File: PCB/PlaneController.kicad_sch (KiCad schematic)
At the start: 13 parts, among them J1 Conn_01x06_Pin, J2 Conn_01x04_Pin, J3 Conn_01x03, M1 Motor_Servo, M2 Motor_Servo, M3 Motor_Servo, M4 Motor_Servo, M5 Motor_Servo

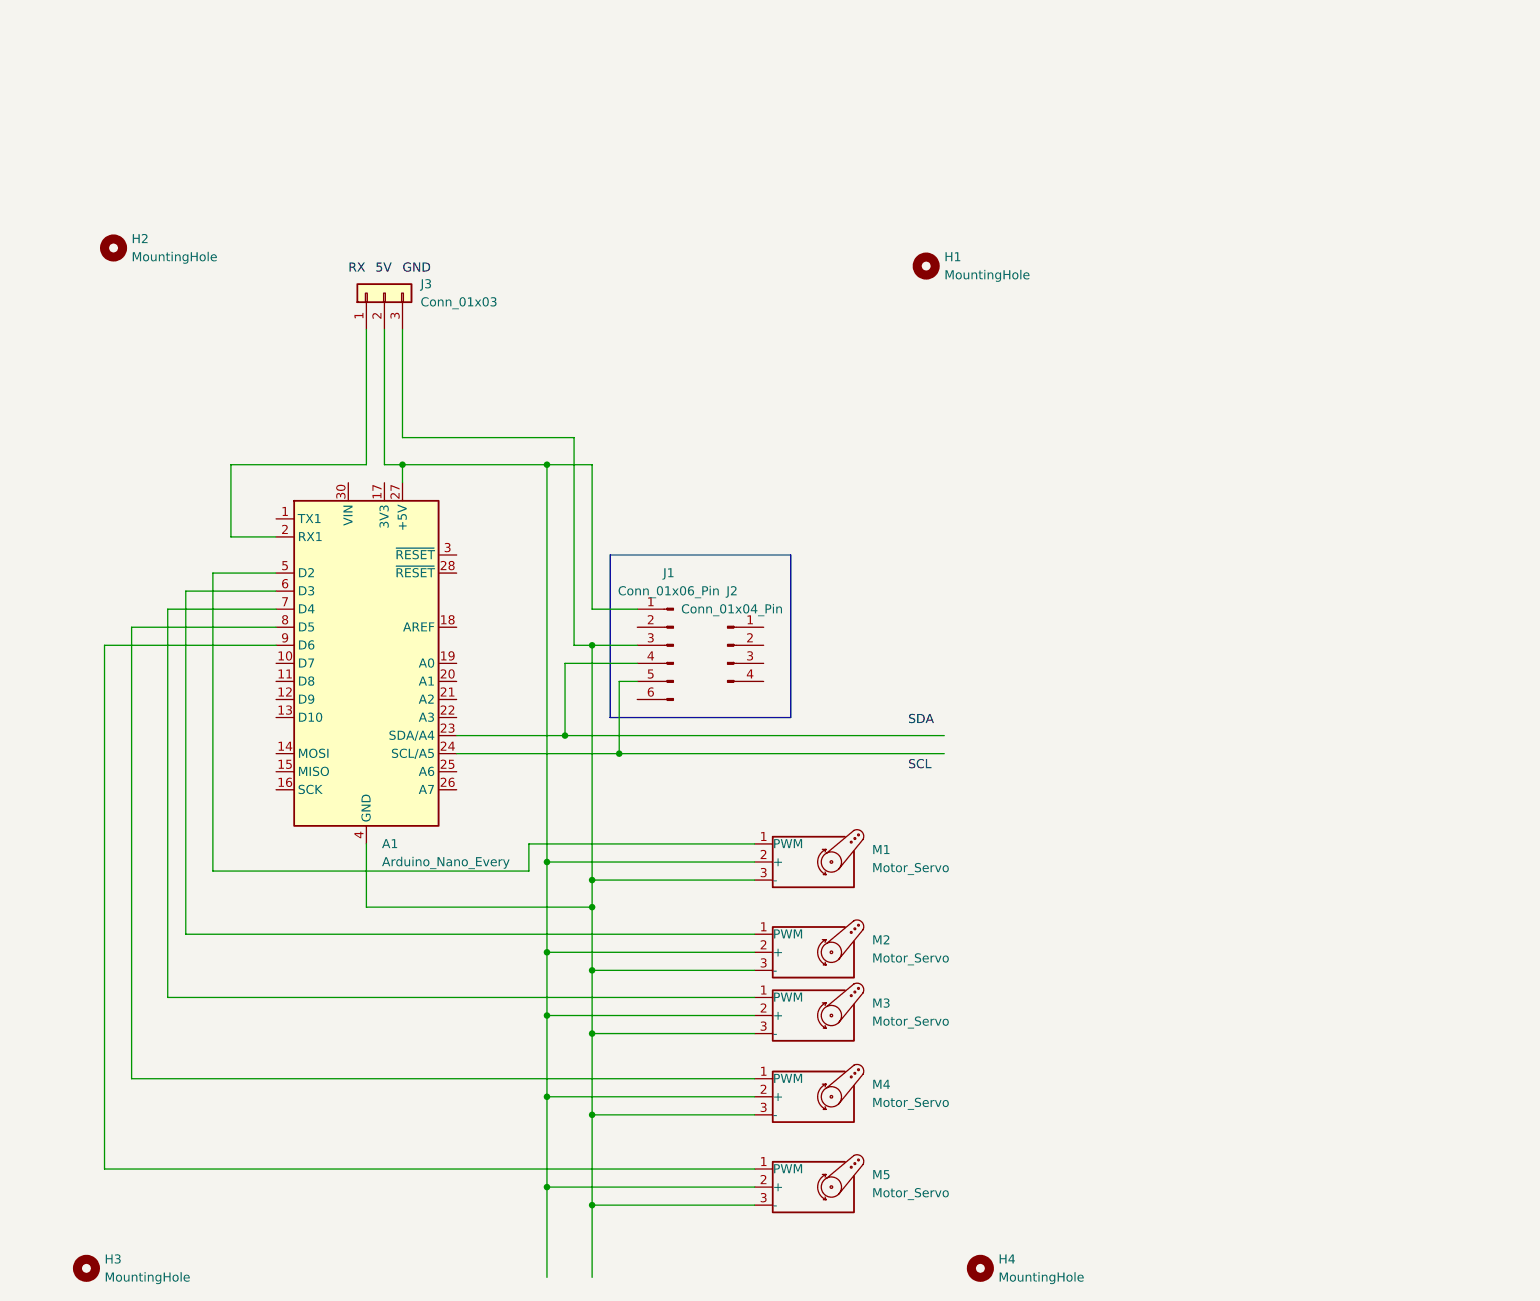
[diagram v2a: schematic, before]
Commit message: Add PCB traces for CC1101 radio
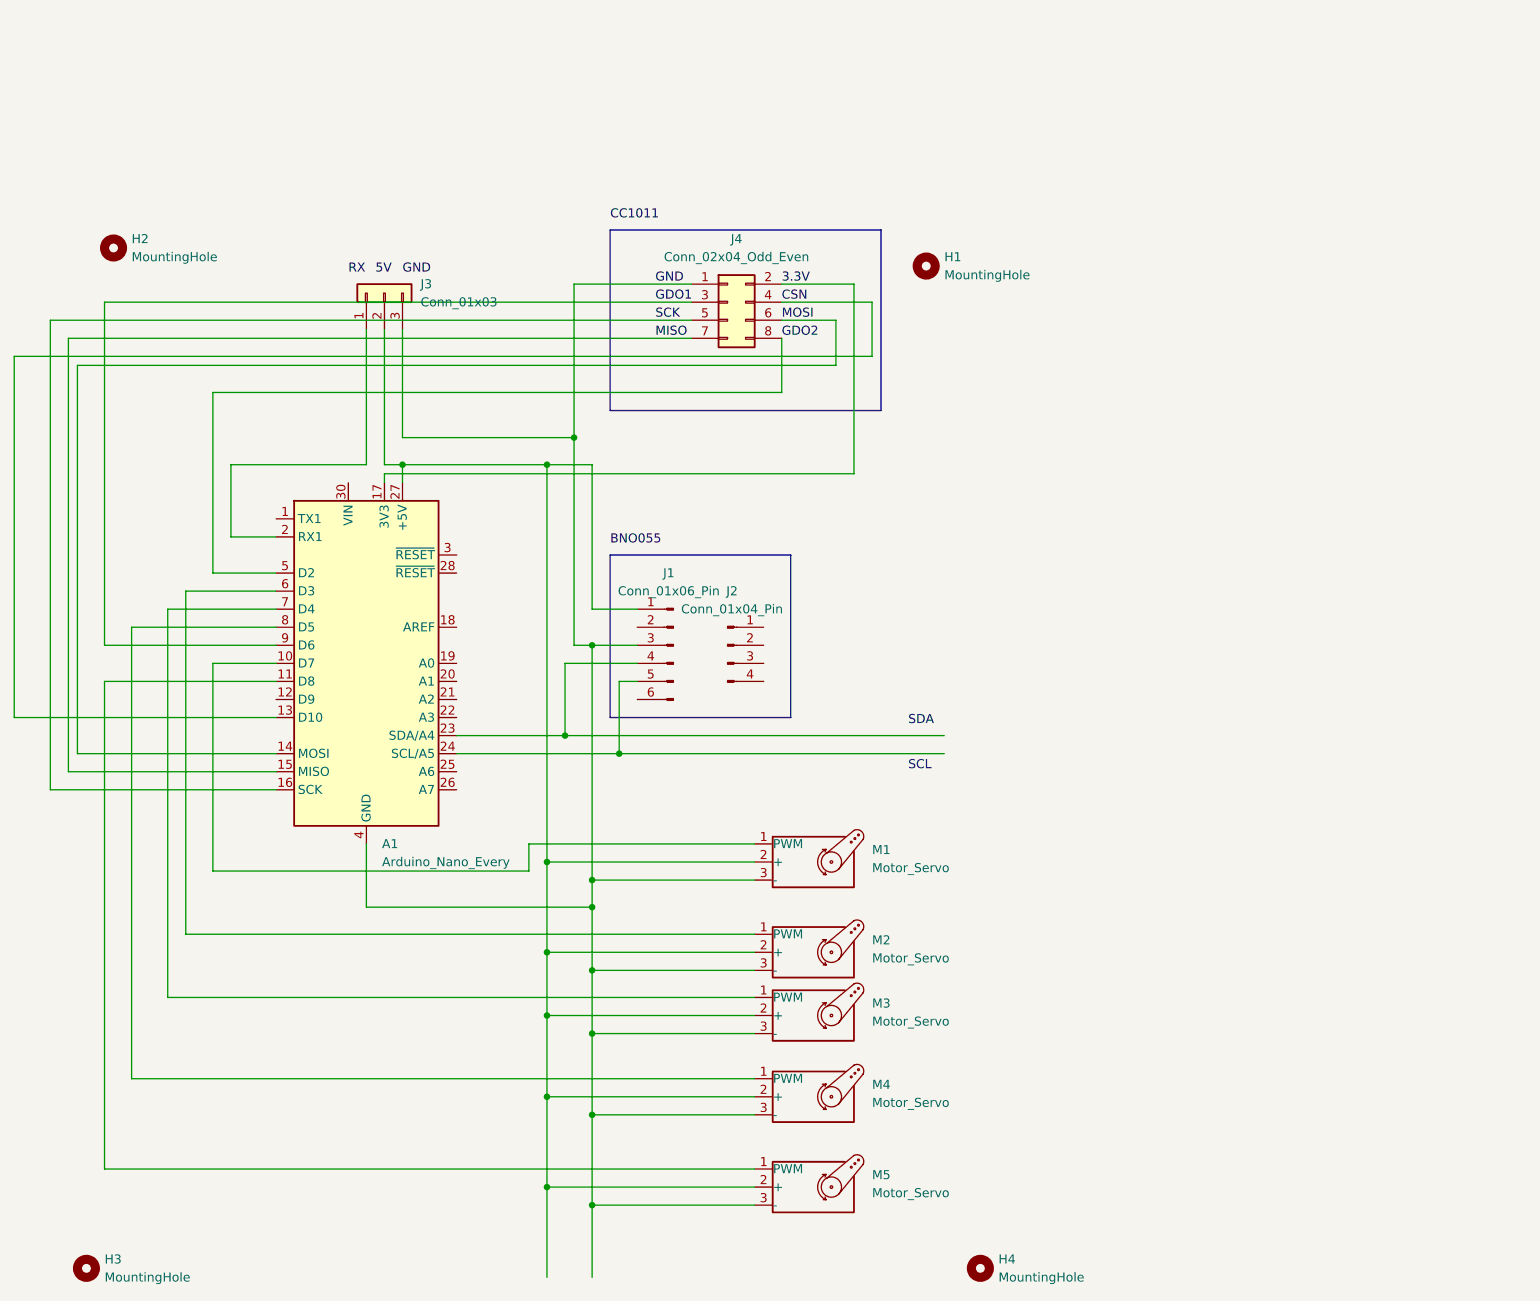
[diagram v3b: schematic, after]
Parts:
- added J4: Conn_02x04_Odd_Even, Connector_PinSocket_2.54mm:PinSocket_2x04_P2.54mm_Vertical, symbol Connector_Generic:Conn_02x04_Odd_Even
- J1: footprint Connector_PinHeader_2.54mm:PinHeader_1x06_P2.54mm_Vertical -> Connector_PinSocket_2.54mm:PinSocket_1x06_P2.54mm_Vertical
- J2: footprint Connector_PinHeader_2.54mm:PinHeader_1x04_P2.54mm_Vertical -> Connector_PinSocket_2.54mm:PinSocket_1x04_P2.54mm_Vertical
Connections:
- net GND: now also A1.29 (GND), A1.4 (GND), J1.3 (Pin_3), J3.3 (Pin_3), M1.3 (-), M2.3 (-), M3.3 (-), M4.3 (-), M5.3 (-), J4.1 (Pin_1)
- net at M5.1 (PWM): now also A1.11 (D8); no longer A1.9 (D6)
- net at M1.1 (PWM): now also A1.10 (D7); no longer A1.5 (D2)
- net CSN: now reaches A1.13 (D10)
- net CSN: now also J4.4 (Pin_4)
- net MOSI: now reaches A1.14 (MOSI)
- net MOSI: now also J4.6 (Pin_6)
- net MISO: now reaches A1.15 (MISO)
- net MISO: now also J4.7 (Pin_7)
- net SCK: now reaches A1.16 (SCK)
- net SCK: now also J4.5 (Pin_5)
- net 3.3V: now reaches A1.17 (3V3)
- net 3.3V: now also J4.2 (Pin_2)
- new net GDO1: A1.9 (D6), J4.3 (Pin_3)
- new net GDO2: A1.5 (D2), J4.8 (Pin_8)

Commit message: Major PCB fix
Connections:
- net GDO1 renamed GDO1 / GDO0
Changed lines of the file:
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@@
-	(wire
-		(pts
-			(xy 118.11 53.34) (xy 35.56 53.34)
-		)
-		(stroke
-			(width 0)
-			(type default)
-		)
-	)
 	(wire
 		(pts
@@
 		(pts
 			(xy 97.79 76.2) (xy 97.79 132.08)
+		)
+		(stroke
+			(width 0)
+			(type default)
+		)
+	)
+	(wire
+		(pts
+			(xy 35.56 53.34) (xy 118.11 53.34)
 		)
 		(stroke
@@
 	)
 	(rectangle
-		(start 106.68 43.18)
+		(start 102.87 43.18)
 		(end 144.78 68.58)
 		(stroke
@@
 	)
 	(label "CC1011"
-		(at 106.68 41.91 0)
+		(at 102.87 41.91 0)
 		(fields_autoplaced yes)
 		(effects
@@
 		)
 	)
-	(label "GDO1"
-		(at 113.03 53.34 0)
-		(fields_autoplaced yes)
-		(effects
+	(label "GDO1 {slash} GDO0"
+		(at 104.14 53.34 0)
+		(fields_autoplaced yes)
+		(effects

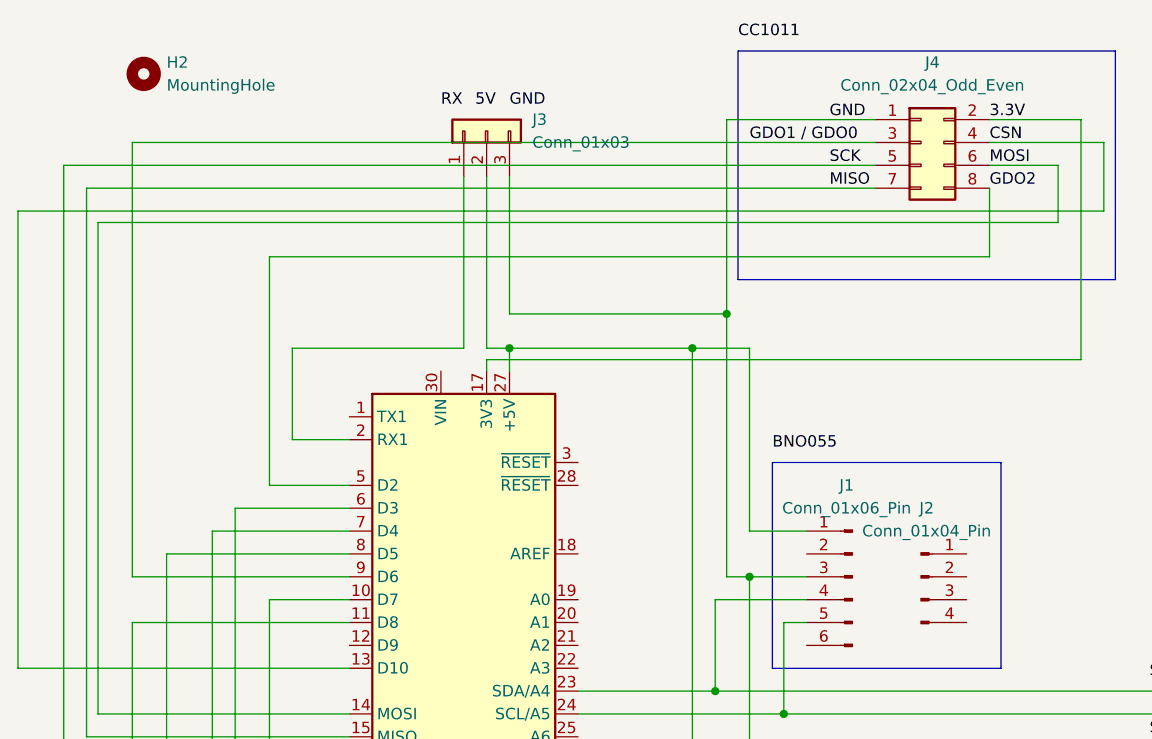
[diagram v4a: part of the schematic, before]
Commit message: Radio is now connected and unnecessary connections are removed from the pcb
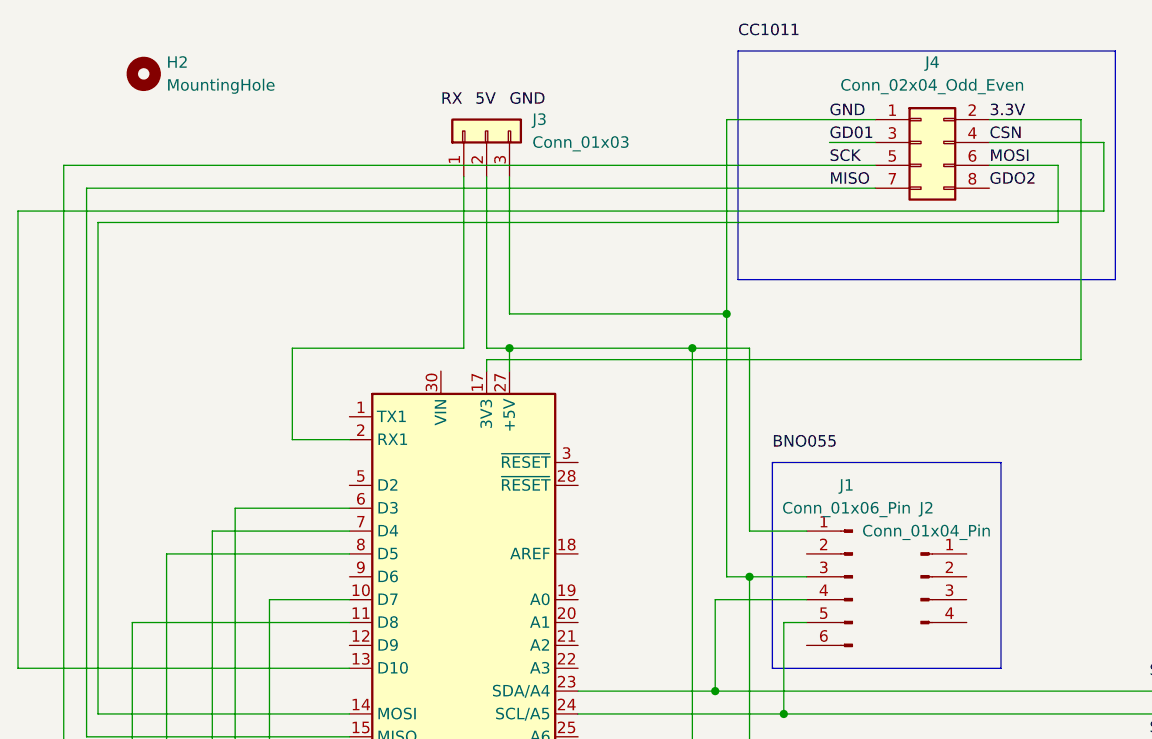
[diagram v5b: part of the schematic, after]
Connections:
- net GDO2: no longer A1.5 (D2)
- net GDO1 / GDO0: no longer names the net of A1.9 (D6)
- net GDO1 / GDO0: no longer J4.3 (Pin_3)
- new net GD01: J4.3 (Pin_3)
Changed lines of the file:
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@@
-	(wire
-		(pts
-			(xy 130.81 58.42) (xy 130.81 66.04)
-		)
-		(stroke
-			(width 0)
-			(type default)
-		)
-	)
 	(wire
 		(pts
@@
 	(wire
 		(pts
-			(xy 35.56 101.6) (xy 59.69 101.6)
-		)
-		(stroke
-			(width 0)
-			(type default)
-		)
-	)
-	(wire
-		(pts
 			(xy 97.79 144.78) (xy 97.79 153.67)
 		)
@@
 	(wire
 		(pts
+			(xy 113.03 53.34) (xy 118.11 53.34)
+		)
+		(stroke
+			(width 0)
+			(type default)
+		)
+	)
+	(wire
+		(pts
 			(xy 104.14 180.34) (xy 127 180.34)
 		)
@@
 	(wire
 		(pts
-			(xy 130.81 66.04) (xy 50.8 66.04)
-		)
-		(stroke
-			(width 0)
-			(type default)
-		)
-	)
-	(wire
-		(pts
 			(xy 101.6 101.6) (xy 104.14 101.6)
 		)
@@
 	(wire
 		(pts
-			(xy 50.8 91.44) (xy 59.69 91.44)
-		)
-		(stroke
-			(width 0)
-			(type default)
-		)
-	)
-	(wire
-		(pts
 			(xy 127 151.13) (xy 44.45 151.13)
 		)
@@
 	(wire
 		(pts
-			(xy 50.8 66.04) (xy 50.8 91.44)
-		)
-		(stroke
-			(width 0)
-			(type default)
-		)
-	)
-	(wire
-		(pts
 			(xy 143.51 60.96) (xy 143.51 53.34)
 		)
@@
 	(wire
 		(pts
-			(xy 35.56 53.34) (xy 35.56 101.6)
-		)
-		(stroke
-			(width 0)
-			(type default)
-		)
-	)
-	(wire
-		(pts
 			(xy 104.14 134.62) (xy 127 134.62)
 		)
@@
 		(pts
 			(xy 97.79 76.2) (xy 97.79 132.08)
-		)
-		(stroke
-			(width 0)
-			(type default)
-		)
-	)
-	(wire
-		(pts
-			(xy 35.56 53.34) (xy 118.11 53.34)
 		)
 		(stroke
@@
 		)
 	)
+	(label "GD01"
+		(at 113.03 53.34 0)
+		(fields_autoplaced yes)
+		(effects
+			(font
+				(size 1.27 1.27)
+			)
+			(justify left bottom)
+		)
+	)
 	(label "MISO"
 		(at 113.03 58.42 0)
@@
 		(fields_autoplaced yes)
 		(effects
-			(font
-				(size 1.27 1.27)
-			)
-			(justify left bottom)
-		)
-	)
-	(label "GDO1 {slash} GDO0"
-		(at 104.14 53.34 0)
-		(fields_autoplaced yes)
-		(effects
